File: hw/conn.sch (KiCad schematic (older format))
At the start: 0 parts

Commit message: hw: start stm page
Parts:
- added SW?: SW_DIP_x04, symbol Switch:SW_DIP_x04
- added XP?: DC-I2C, symbol dronecode_con:DC-I2C
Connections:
- new net +5V: XP?.1 (Vcc)
- new net CFG_ID0: SW?.1
- new net CFG_ID1: SW?.2
- new net CFG_ID2: SW?.3
- new net GND: SW?.5, SW?.6, SW?.7, SW?.8, XP?.4 (GND)
- new net RPI_SCL: XP?.1 (Vcc)
- new net RPI_SDA: XP?.3 (SDA)
- new net ~HAT_ID_WE: SW?.4
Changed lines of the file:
@@
 Comment4 ""
 $EndDescr
+$Comp
+L Switch:SW_DIP_x04 SW?
+U 1 1 5AC0CE65
+P 3750 2000
+F 0 "SW?" H 3750 2467 50  0000 C CNN
+F 1 "SW_DIP_x04" H 3750 2376 50  0000 C CNN
+F 2 "" H 3750 2000 50  0001 C CNN
+F 3 "" H 3750 2000 50  0001 C CNN
+	1    3750 2000
+	1    0    0    -1
+$EndComp
+Text GLabel 2650 1800 0    60   UnSpc ~ 0
+CFG_ID0
+Text GLabel 2650 1900 0    60   UnSpc ~ 0
+CFG_ID1
+Wire Wire Line
+	3450 1800 2650 1800
+Wire Wire Line
+	2650 1900 3450 1900
+$Comp
+L power:GND #PWR?
+U 1 1 5AC0D0C3
+P 4150 2250
+F 0 "#PWR?" H 4150 2000 50  0001 C CNN
+F 1 "GND" H 4155 2077 50  0000 C CNN
+F 2 "" H 4150 2250 50  0001 C CNN
+F 3 "" H 4150 2250 50  0001 C CNN
+	1    4150 2250
+	1    0    0    -1
+$EndComp
+Wire Wire Line
+	4050 1800 4150 1800
+Wire Wire Line
+	4150 1800 4150 1900
+Wire Wire Line
+	4050 1900 4150 1900
+Connection ~ 4150 1900
+Wire Wire Line
+	4150 1900 4150 2000
+Wire Wire Line
+	4050 2000 4150 2000
+Connection ~ 4150 2000
+Wire Wire Line
+	4150 2000 4150 2100
+Wire Wire Line
+	4050 2100 4150 2100
+Connection ~ 4150 2100
+Wire Wire Line
+	4150 2100 4150 2250
+Text GLabel 2650 2100 0    60   UnSpc ~ 0
+~HAT_ID_WE
+Wire Wire Line
+	2650 2100 3450 2100
+Text GLabel 2650 2000 0    60   UnSpc ~ 0
+CFG_ID2
+Wire Wire Line
+	2650 2000 3450 2000
+Text GLabel 3500 4700 2    60   Output ~ 0
+RPI_TX
+Text GLabel 3500 4800 2    60   Input ~ 0
+RPI_RX
+Text GLabel 3500 5350 2    60   Output ~ 0
+BCM20_SPI1_MOSI
+Text GLabel 3500 5450 2    60   Output ~ 0
+BCM21_SPI1_SCLK
+Text GLabel 3500 5250 2    60   Output ~ 0
+~RPI_SPI1_CE2
+Text GLabel 3500 5050 2    60   BiDi ~ 0
+BCM12
+Text GLabel 3100 3250 0    60   BiDi ~ 0
+RPI_SCL
+Text GLabel 3100 3350 0    60   BiDi ~ 0
+RPI_SDA
+Text GLabel 3000 5350 0    60   Input ~ 0
+BCM19_SPI1_MISO
+Text GLabel 3000 5450 0    60   Output ~ 0
+BCM26
+Text GLabel 3000 5250 0    60   BiDi ~ 0
+BCM13
+Text GLabel 3000 5050 0    60   BiDi ~ 0
+BCM5
+Text GLabel 3000 5150 0    60   BiDi ~ 0
+BCM6
+$Comp
+L dronecode_con:DC-I2C XP?
+U 1 1 5AC44595
+P 3800 3300
+F 0 "XP?" H 4027 3353 60  0000 L CNN
+F 1 "DC-I2C" H 4027 3247 60  0000 L CNN
+F 2 "" H 3800 3300 60  0001 C CNN
+F 3 "https://wiki.dronecode.org/workgroup/connectors/start" H 3800 3300 60  0001 C CNN
+	1    3800 3300
+	1    0    0    -1
+$EndComp
+Wire Wire Line
+	3100 3250 3400 3250
+Wire Wire Line
+	3100 3350 3400 3350
+$Comp
+L power:GND #PWR?
+U 1 1 5AC44B9B
+P 3300 3550
+F 0 "#PWR?" H 3300 3300 50  0001 C CNN
+F 1 "GND" H 3305 3377 50  0000 C CNN
+F 2 "" H 3300 3550 50  0001 C CNN
+F 3 "" H 3300 3550 50  0001 C CNN
+	1    3300 3550
+	1    0    0    -1
+$EndComp
+$Comp
+L power:+5V #PWR?
+U 1 1 5AC44BF4
+P 3300 3050
+F 0 "#PWR?" H 3300 2900 50  0001 C CNN
+F 1 "+5V" H 3315 3223 50  0000 C CNN
+F 2 "" H 3300 3050 50  0001 C CNN
+F 3 "" H 3300 3050 50  0001 C CNN
+	1    3300 3050
+	1    0    0    -1
+$EndComp
+Wire Wire Line
+	3400 3150 3300 3150
+Wire Wire Line
+	3300 3150 3300 3050
+Wire Wire Line
+	3300 3550 3300 3450
+Wire Wire Line
+	3300 3450 3400 3450
+Text GLabel 3200 6500 0    60   Output ~ 0
+SERVO0
+Text GLabel 3200 6600 0    60   Output ~ 0
+SERVO1
+Text GLabel 3200 6700 0    60   Output ~ 0
+SERVO2
+Text GLabel 3200 6800 0    60   Output ~ 0
+SERVO3
 $EndSCHEMATC

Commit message: hw: update libs
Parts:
- XP?: symbol dronecode_con:DC-I2C -> dronecode-conn:DC-I2C
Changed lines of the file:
@@
 BCM6
 $Comp
-L dronecode_con:DC-I2C XP?
+L dronecode-conn:DC-I2C XP?
 U 1 1 5AC44595
 P 3800 3300

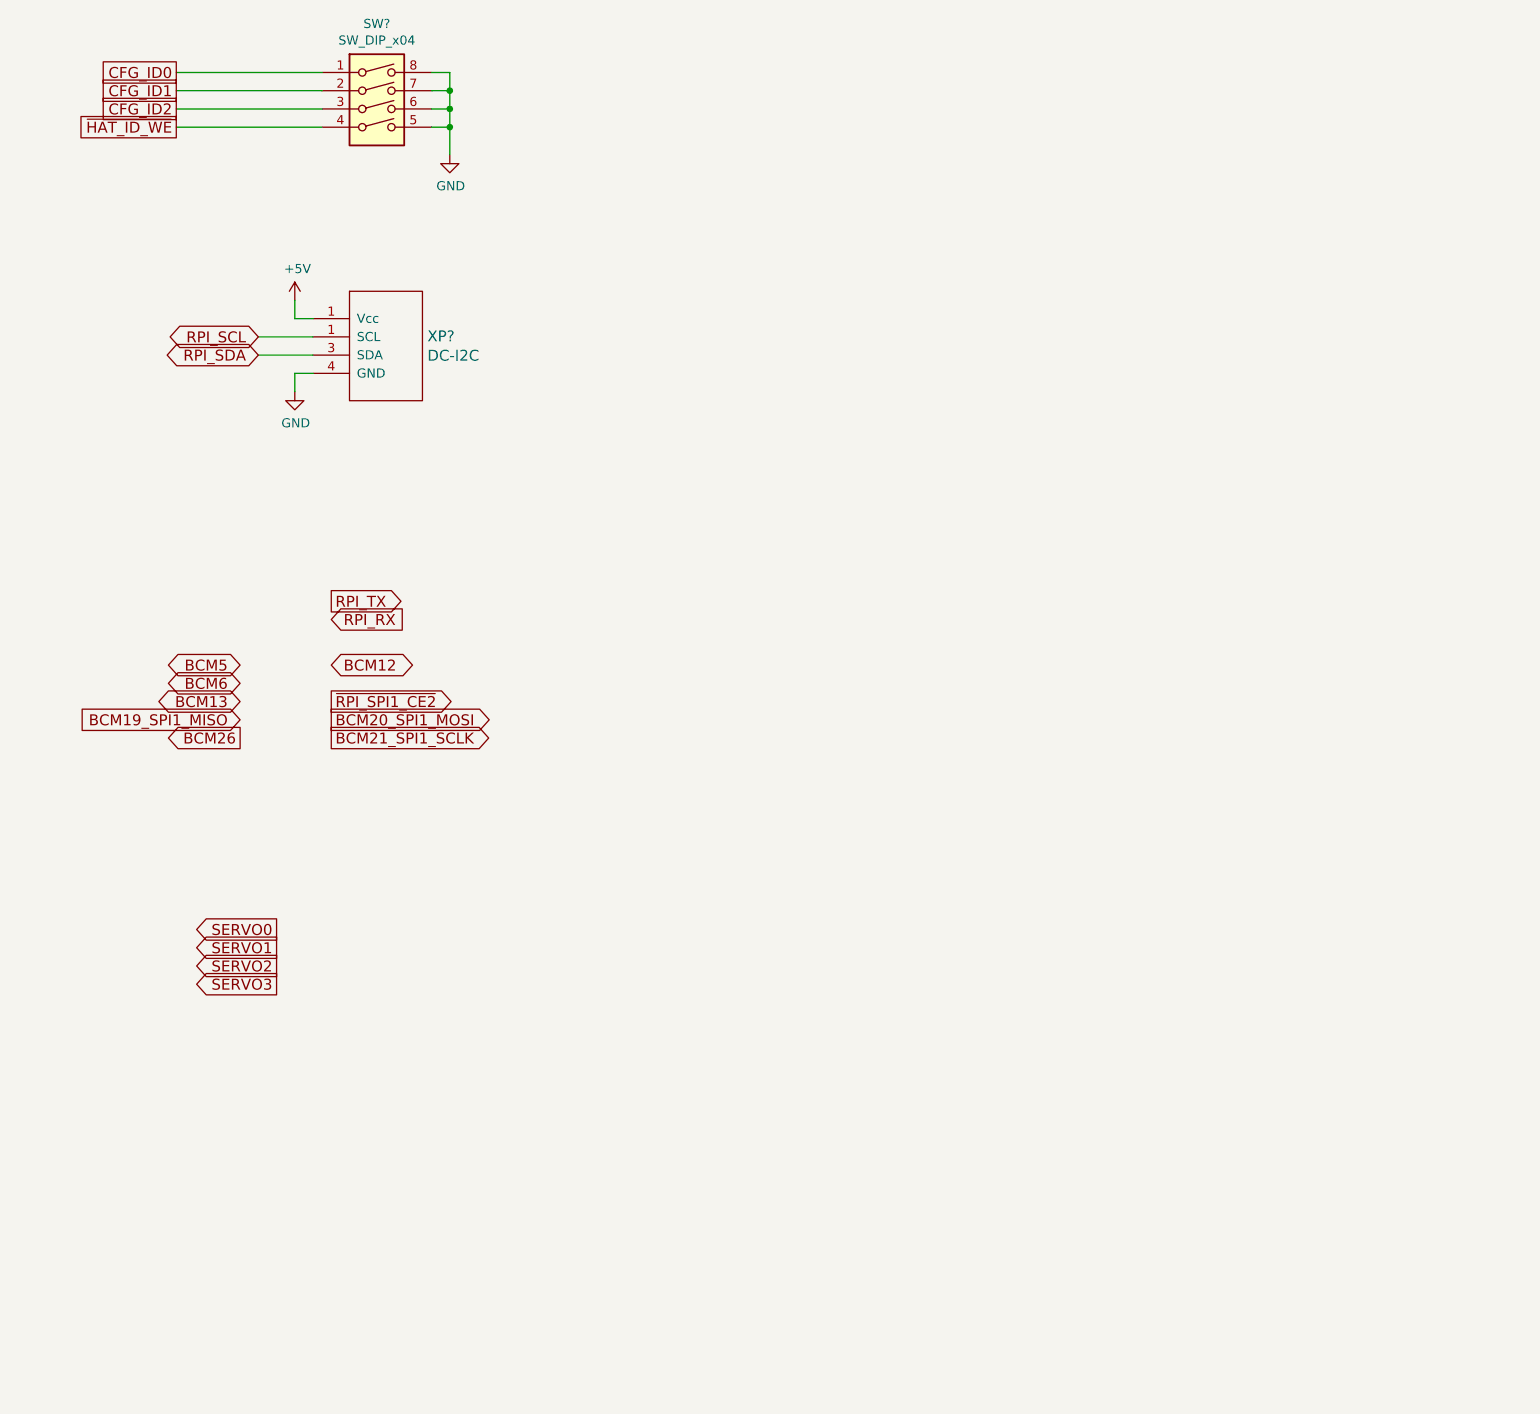
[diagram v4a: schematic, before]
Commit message: hw: finish conn page
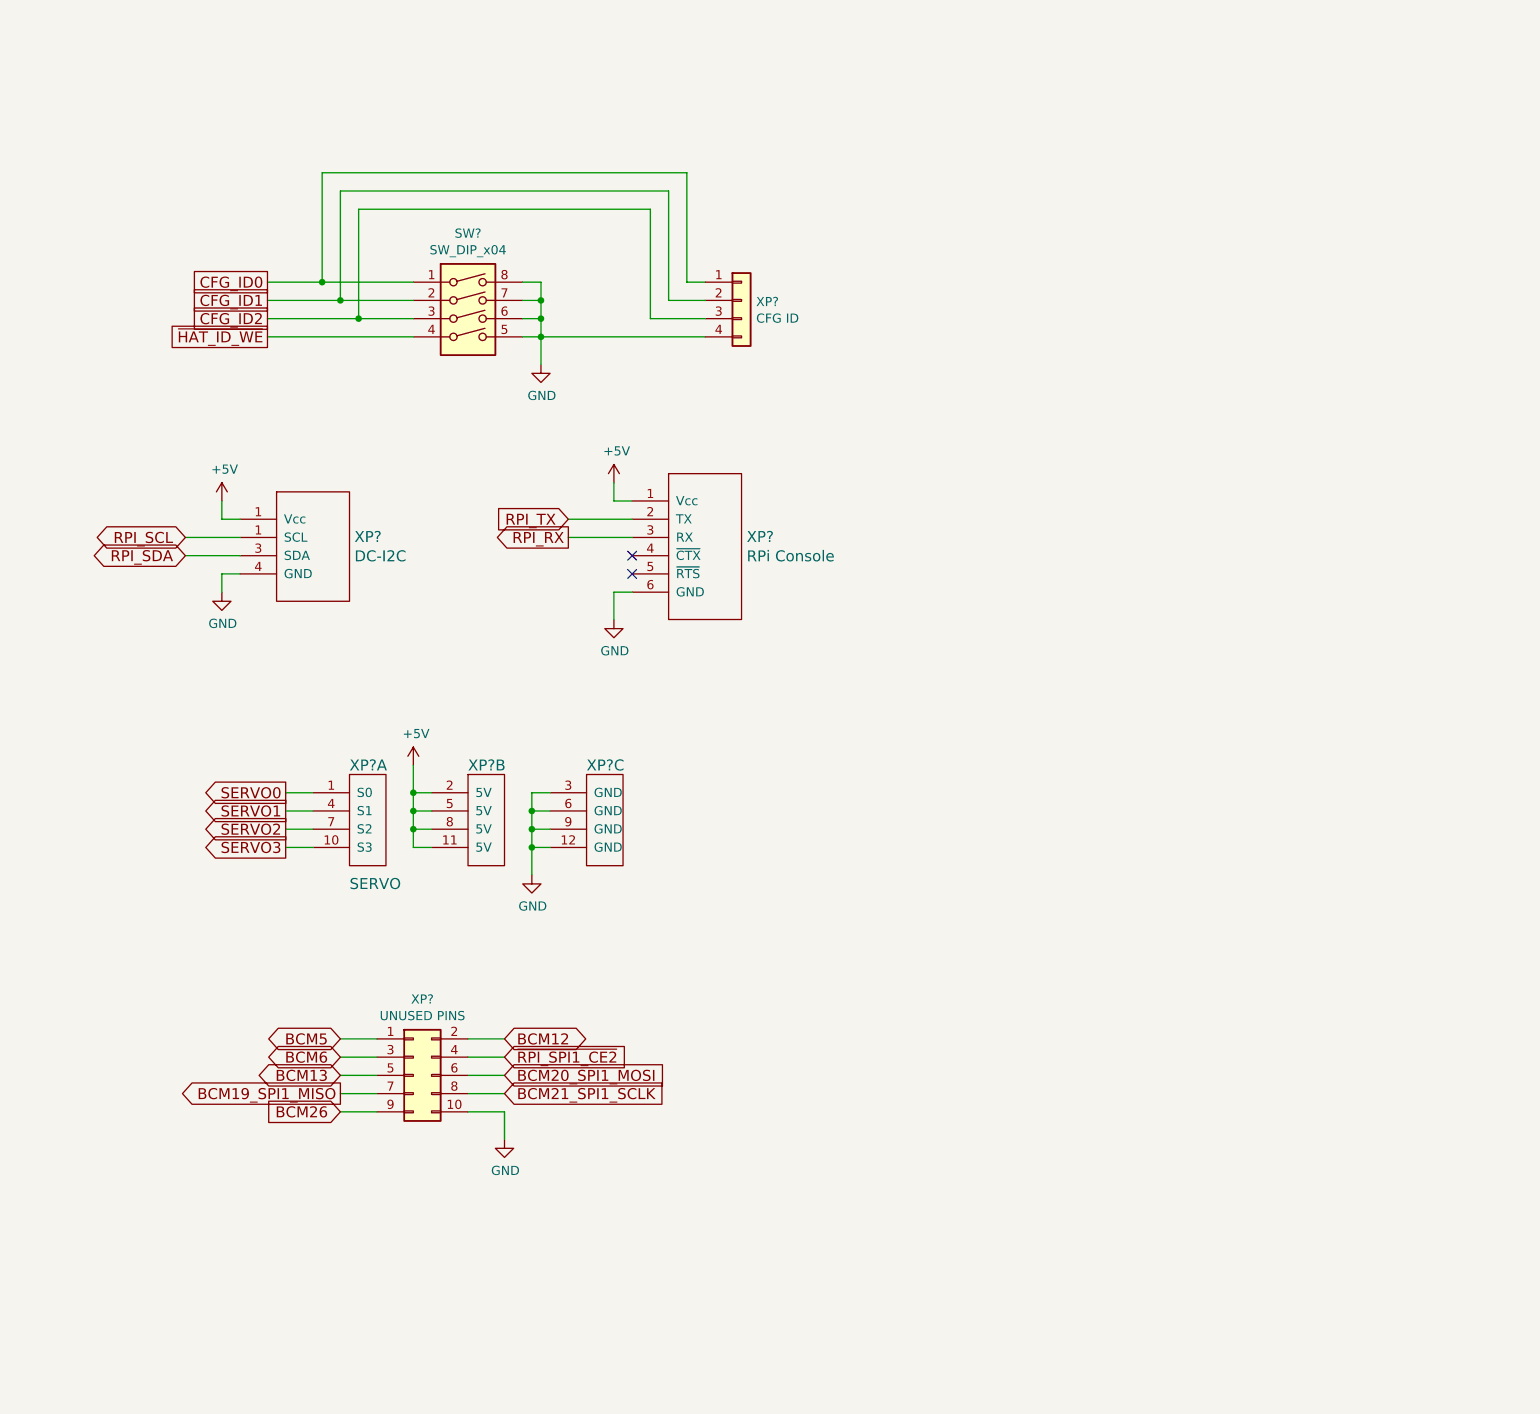
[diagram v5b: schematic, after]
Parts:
- added XP?: SERVO, symbol dronecode-conn:Servo-Conn4
- added XP? (x2): Servo-Conn4, symbol dronecode-conn:Servo-Conn4
- added XP?: CFG ID, symbol Connector_Generic:Conn_01x04
- added XP?: RPi Console, symbol dronecode-conn:DC-Telemetry
- added XP?: UNUSED PINS, symbol Connector_Generic:Conn_02x05_Odd_Even
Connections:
- net +5V: now also XP?.1 (Vcc), XP?.11 (5V), XP?.2 (5V), XP?.5 (5V), XP?.8 (5V)
- net BCM12: now also XP?.2 (Pin_2)
- net BCM13: now also XP?.5 (Pin_5)
- net BCM19_SPI1_MISO: now also XP?.7 (Pin_7)
- net BCM20_SPI1_MOSI: now also XP?.6 (Pin_6)
- net BCM21_SPI1_SCLK: now also XP?.8 (Pin_8)
- net BCM26: now also XP?.9 (Pin_9)
- net BCM5: now also XP?.1 (Pin_1)
- net BCM6: now also XP?.3 (Pin_3)
- net CFG_ID0: now also XP?.1 (Pin_1)
- net CFG_ID1: now also XP?.2 (Pin_2)
- net CFG_ID2: now also XP?.3 (Pin_3)
- net GND: now also XP?.10 (Pin_10), XP?.12 (GND), XP?.3 (GND), XP?.4 (Pin_4), XP?.6 (GND), XP?.6 (GND), XP?.9 (GND)
- net RPI_RX: now also XP?.3 (RX)
- net RPI_TX: now also XP?.2 (TX)
- net SERVO0: now also XP?.1 (S0)
- net SERVO1: now also XP?.4 (S1)
- net SERVO2: now also XP?.7 (S2)
- net SERVO3: now also XP?.10 (S3)
- net ~RPI_SPI1_CE2: now also XP?.4 (Pin_4)
- no-connect marks 0 -> 2
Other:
- moved on the sheet: SW?, XP?
